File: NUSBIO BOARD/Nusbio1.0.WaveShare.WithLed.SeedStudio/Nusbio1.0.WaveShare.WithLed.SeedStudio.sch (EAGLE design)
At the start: 7 parts

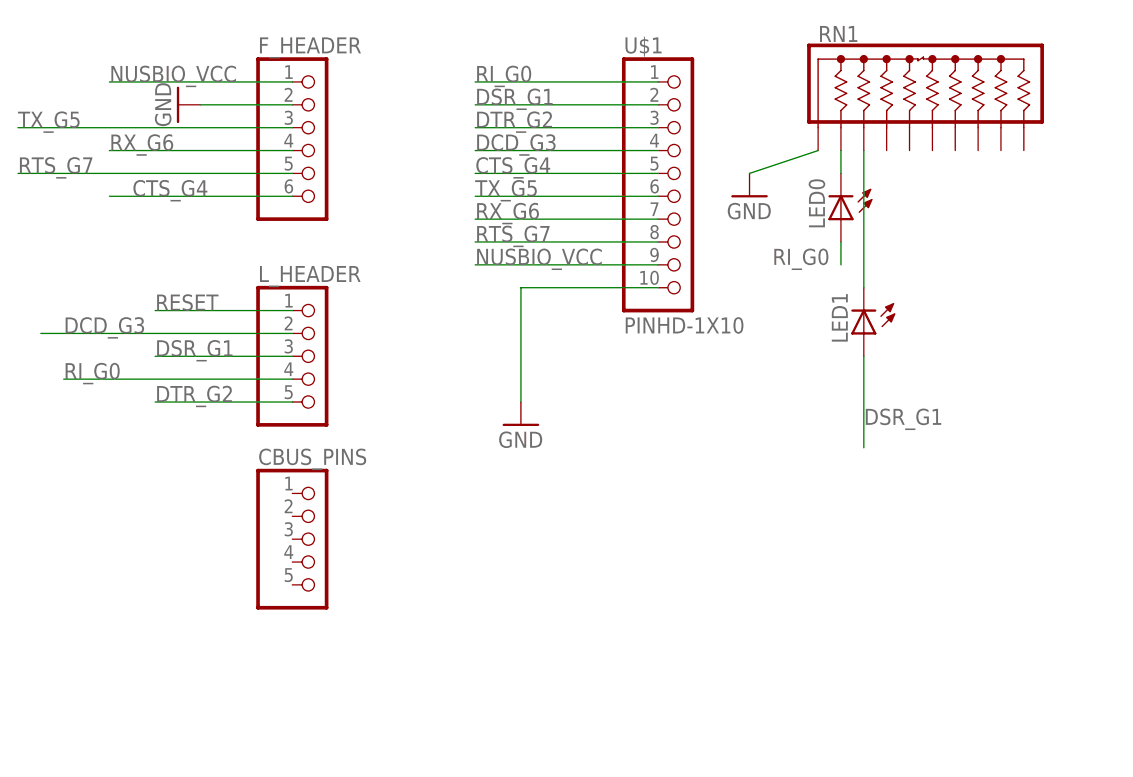
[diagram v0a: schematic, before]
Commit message: New board Nusbio WaveShare SeedStudio edition larger with 8 blue 1206 led
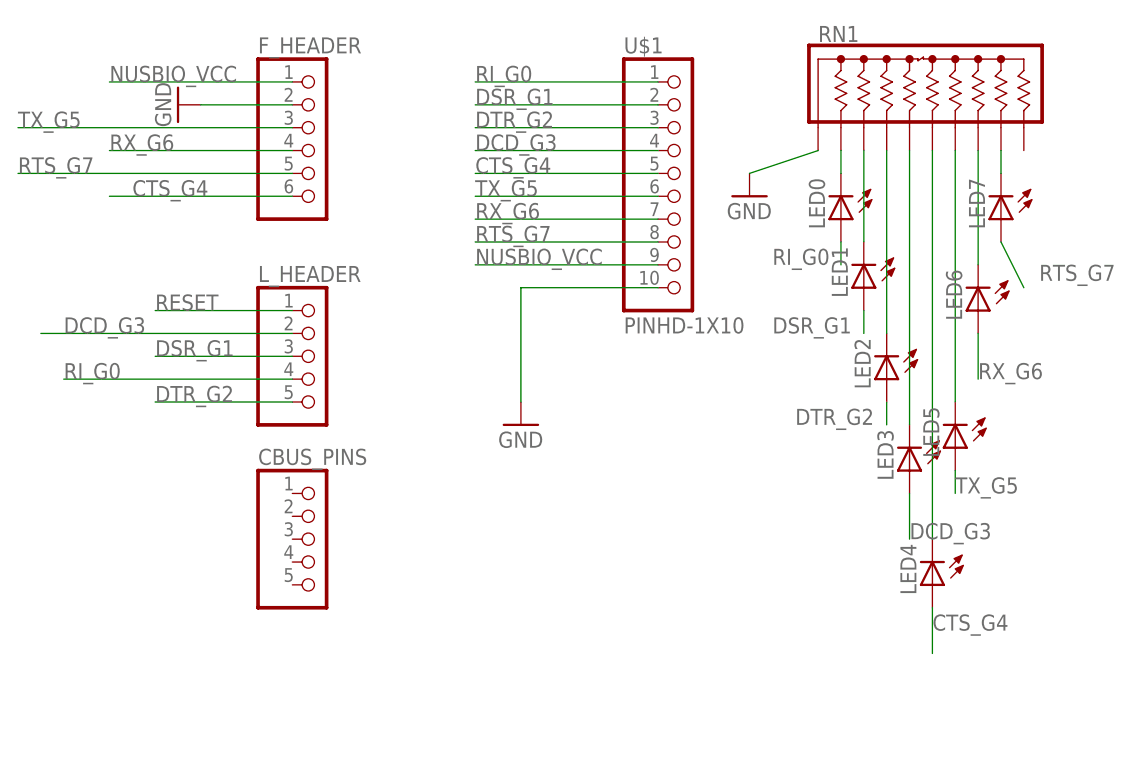
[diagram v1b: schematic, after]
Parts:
- added LED2, LED3, LED4, LED5, LED6, LED7: (no value), adafruit:LEDSMT1206
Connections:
- new net N$3: LED2.C, RN1.4
- new net N$4: LED3.C, RN1.5
- new net N$5: LED4.C, RN1.6
- new net N$6: LED7.C, RN1.9
- new net N$7: LED5.C, RN1.7
- new net N$8: LED6.C, RN1.8
- net CTS_G4: now also LED4.A
- net DCD_G3: now also LED3.A
- net DTR_G2: now also LED2.A
- net RTS_G7: now also LED7.A
- net RX_G6: now also LED6.A
- net TX_G5: now also LED5.A
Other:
- moved on the sheet: LED1
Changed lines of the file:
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@@
 <part name="LED0" library="adafruit" deviceset="LED" device="SMT1206"/>
 <part name="LED1" library="adafruit" deviceset="LED" device="SMT1206"/>
+<part name="LED2" library="adafruit" deviceset="LED" device="SMT1206"/>
+<part name="LED3" library="adafruit" deviceset="LED" device="SMT1206"/>
+<part name="LED4" library="adafruit" deviceset="LED" device="SMT1206"/>
+<part name="LED7" library="adafruit" deviceset="LED" device="SMT1206"/>
+<part name="LED6" library="adafruit" deviceset="LED" device="SMT1206"/>
+<part name="LED5" library="adafruit" deviceset="LED" device="SMT1206"/>
 </parts>
 <sheets>
@@
 <instance part="GND3" gate="1" x="144.78" y="71.12"/>
 <instance part="LED0" gate="G$1" x="154.94" y="68.58" rot="R180"/>
-<instance part="LED1" gate="G$1" x="157.48" y="55.88" rot="R180"/>
+<instance part="LED1" gate="G$1" x="157.48" y="60.96" rot="R180"/>
+<instance part="LED2" gate="G$1" x="160.02" y="50.8" rot="R180"/>
+<instance part="LED3" gate="G$1" x="162.56" y="40.64" rot="R180"/>
+<instance part="LED4" gate="G$1" x="165.1" y="27.94" rot="R180"/>
+<instance part="LED7" gate="G$1" x="172.72" y="68.58" rot="R180"/>
+<instance part="LED6" gate="G$1" x="170.18" y="58.42" rot="R180"/>
+<instance part="LED5" gate="G$1" x="167.64" y="43.18" rot="R180"/>
 </instances>
 <busses>
@@
 <label x="114.3" y="71.12" size="1.778" layer="95"/>
 </segment>
+<segment>
+<pinref part="LED5" gate="G$1" pin="A"/>
+<wire x1="167.64" y1="40.64" x2="167.64" y2="38.1" width="0.1524" layer="91"/>
+<label x="167.64" y="38.1" size="1.778" layer="95"/>
+</segment>
 </net>
 <net name="RX_G6" class="0">
@@
 <label x="114.3" y="68.58" size="1.778" layer="95"/>
 </segment>
+<segment>
+<pinref part="LED6" gate="G$1" pin="A"/>
+<wire x1="170.18" y1="55.88" x2="170.18" y2="50.8" width="0.1524" layer="91"/>
+<label x="170.18" y="50.8" size="1.778" layer="95"/>
+</segment>
 </net>
 <net name="RTS_G7" class="0">
@@
 <label x="114.3" y="66.04" size="1.778" layer="95"/>
 </segment>
+<segment>
+<pinref part="LED7" gate="G$1" pin="A"/>
+<wire x1="172.72" y1="66.04" x2="175.26" y2="60.96" width="0.1524" layer="91"/>
+<label x="185.42" y="63.5" size="1.778" layer="95" rot="R180"/>
+</segment>
 </net>
 <net name="CTS_G4" class="0">
@@
 <label x="114.3" y="73.66" size="1.778" layer="95"/>
 </segment>
+<segment>
+<pinref part="LED4" gate="G$1" pin="A"/>
+<wire x1="165.1" y1="25.4" x2="165.1" y2="20.32" width="0.1524" layer="91"/>
+<label x="165.1" y="22.86" size="1.778" layer="95"/>
+</segment>
 </net>
 <net name="RESET" class="0">
@@
 <label x="114.3" y="76.2" size="1.778" layer="95"/>
 </segment>
+<segment>
+<pinref part="LED3" gate="G$1" pin="A"/>
+<wire x1="162.56" y1="38.1" x2="162.56" y2="33.02" width="0.1524" layer="91"/>
+<label x="162.56" y="33.02" size="1.778" layer="95"/>
+</segment>
 </net>
 <net name="DSR_G1" class="0">
@@
 <segment>
 <pinref part="LED1" gate="G$1" pin="A"/>
-<wire x1="157.48" y1="53.34" x2="157.48" y2="43.18" width="0.1524" layer="91"/>
-<label x="157.48" y="45.72" size="1.778" layer="95"/>
+<wire x1="157.48" y1="58.42" x2="157.48" y2="55.88" width="0.1524" layer="91"/>
+<label x="147.32" y="55.88" size="1.778" layer="95"/>
 </segment>
 </net>
@@
 <label x="114.3" y="78.74" size="1.778" layer="95"/>
 </segment>
+<segment>
+<pinref part="LED2" gate="G$1" pin="A"/>
+<wire x1="160.02" y1="48.26" x2="160.02" y2="45.72" width="0.1524" layer="91"/>
+<label x="149.86" y="45.72" size="1.778" layer="95"/>
+</segment>
 </net>
 <net name="N$2" class="0">
@@
 <pinref part="LED1" gate="G$1" pin="C"/>
 <pinref part="RN1" gate="G$1" pin="3"/>
-<wire x1="157.48" y1="60.96" x2="157.48" y2="76.2" width="0.1524" layer="91"/>
-</segment>
-</net>
+<wire x1="157.48" y1="66.04" x2="157.48" y2="76.2" width="0.1524" layer="91"/>
+</segment>
+</net>
+<net name="N$3" class="0">
+<segment>
+<pinref part="LED2" gate="G$1" pin="C"/>
+<pinref part="RN1" gate="G$1" pin="4"/>
+<wire x1="160.02" y1="55.88" x2="160.02" y2="76.2" width="0.1524" layer="91"/>
+</segment>
+</net>
+<net name="N$4" class="0">
+<segment>
+<pinref part="LED3" gate="G$1" pin="C"/>
+<pinref part="RN1" gate="G$1" pin="5"/>
+<wire x1="162.56" y1="45.72" x2="162.56" y2="76.2" width="0.1524" layer="91"/>
+</segment>
+</net>
+<net name="N$5" class="0">
+<segment>
+<pinref part="LED4" gate="G$1" pin="C"/>
+<pinref part="RN1" gate="G$1" pin="6"/>
+<wire x1="165.1" y1="33.02" x2="165.1" y2="76.2" width="0.1524" layer="91"/>
+</segment>
+</net>
+<net name="N$6" class="0">
+<segment>
+<pinref part="LED7" gate="G$1" pin="C"/>
+<pinref part="RN1" gate="G$1" pin="9"/>
+<wire x1="172.72" y1="73.66" x2="172.72" y2="76.2" width="0.1524" layer="91"/>
+</segment>
+</net>
+<net name="N$8" class="0">
+<segment>
+<pinref part="LED6" gate="G$1" pin="C"/>
+<pinref part="RN1" gate="G$1" pin="8"/>
+<wire x1="170.18" y1="63.5" x2="170.18" y2="76.2" width="0.1524" layer="91"/>
+</segment>
+</net>
+<net name="N$7" class="0">
+<segment>
+<pinref part="LED5" gate="G$1" pin="C"/>
+<pinref part="RN1" gate="G$1" pin="7"/>
+<wire x1="167.64" y1="48.26" x2="167.64" y2="76.2" width="0.1524" layer="91"/>
+</segment>
+</net>

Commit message: New board Nusbio WaveShare SeedStudio edition larger with 8 blue 1206 led
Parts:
- added LPOWER: (no value), adafruit:LEDSMT1206
- added RPWR: (no value), adafruit:R-US_R1206
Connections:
- new net N$9: LPOWER.C, RPWR.1
- net GND: now also RPWR.2
- net NUSBIO_VCC: now also LPOWER.A
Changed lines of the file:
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@@
 <part name="LED6" library="adafruit" deviceset="LED" device="SMT1206"/>
 <part name="LED5" library="adafruit" deviceset="LED" device="SMT1206"/>
+<part name="LPOWER" library="adafruit" deviceset="LED" device="SMT1206"/>
+<part name="RPWR" library="adafruit" deviceset="R-US_" device="R1206"/>
+<part name="GND4" library="supply1" deviceset="GND" device=""/>
 </parts>
 <sheets>
@@
 <instance part="LED6" gate="G$1" x="170.18" y="58.42" rot="R180"/>
 <instance part="LED5" gate="G$1" x="167.64" y="43.18" rot="R180"/>
+<instance part="LPOWER" gate="G$1" x="139.7" y="15.24" rot="R180"/>
+<instance part="RPWR" gate="G$1" x="132.08" y="33.02" rot="R90"/>
+<instance part="GND4" gate="1" x="132.08" y="45.72" rot="R180"/>
 </instances>
 <busses>
@@
 <wire x1="144.78" y1="73.66" x2="152.4" y2="76.2" width="0.1524" layer="91"/>
 </segment>
+<segment>
+<pinref part="RPWR" gate="G$1" pin="2"/>
+<pinref part="GND4" gate="1" pin="GND"/>
+<wire x1="132.08" y1="38.1" x2="132.08" y2="43.18" width="0.1524" layer="91"/>
+</segment>
 </net>
 <net name="NUSBIO_VCC" class="0">
@@
 <label x="73.66" y="83.82" size="1.778" layer="95"/>
 </segment>
+<segment>
+<pinref part="LPOWER" gate="G$1" pin="A"/>
+<wire x1="139.7" y1="12.7" x2="132.08" y2="10.16" width="0.1524" layer="91"/>
+<label x="137.16" y="12.7" size="1.778" layer="95"/>
+</segment>
 </net>
 <net name="TX_G5" class="0">
@@
 </segment>
 </net>
+<net name="N$9" class="0">
+<segment>
+<pinref part="LPOWER" gate="G$1" pin="C"/>
+<pinref part="RPWR" gate="G$1" pin="1"/>
+<wire x1="139.7" y1="20.32" x2="132.08" y2="27.94" width="0.1524" layer="91"/>
+</segment>
+</net>
